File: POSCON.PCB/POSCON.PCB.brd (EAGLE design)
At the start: 55.8 x 40.9 mm, 21 parts, among them J1-PROG RJ45-8, J2 RJ45-8, U1 MC9S08QG-DT, U3 RS485SOIC, U4 PCA9552

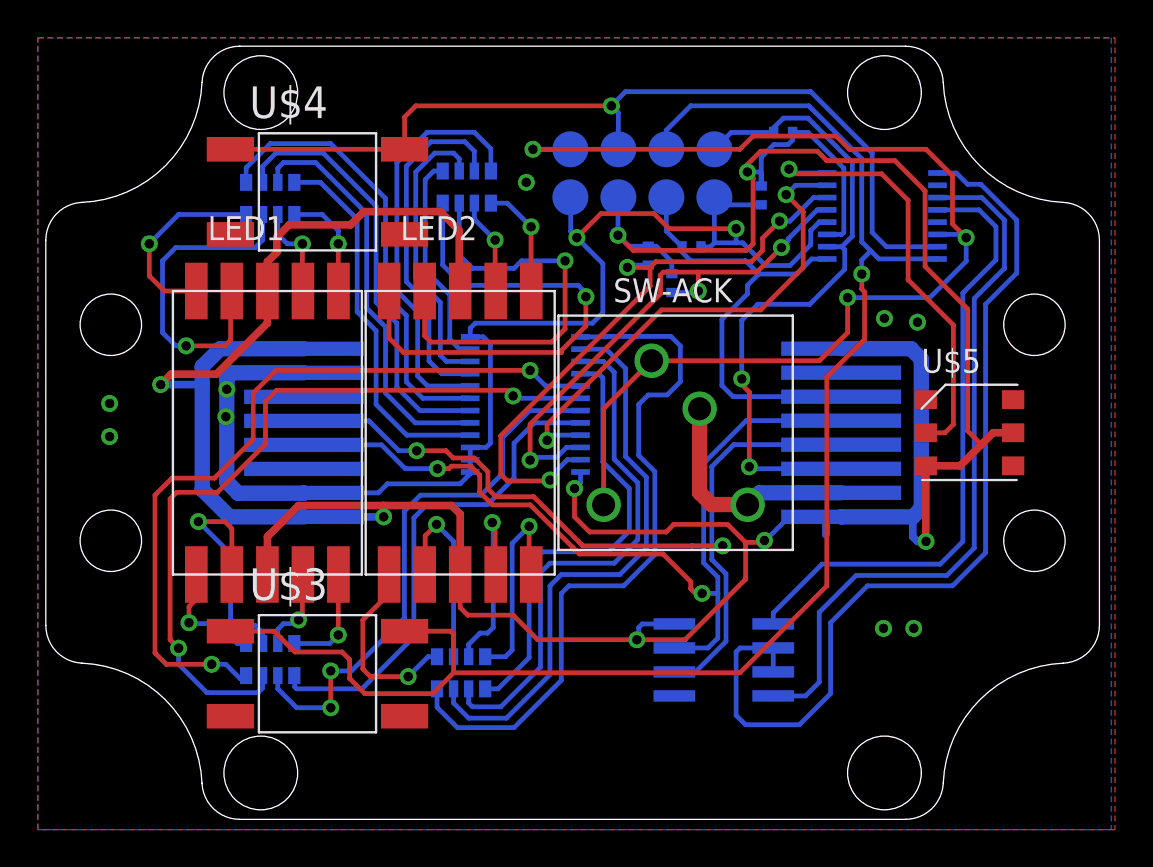
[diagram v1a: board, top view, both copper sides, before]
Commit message: KW2 antenna, LasCon panel, PosCon fiducials
Added vertical MMCX connector to KW2 design & library; added panelized
version of LasCon (old and new design); added Adafruit library and
fiducials to new PosCon
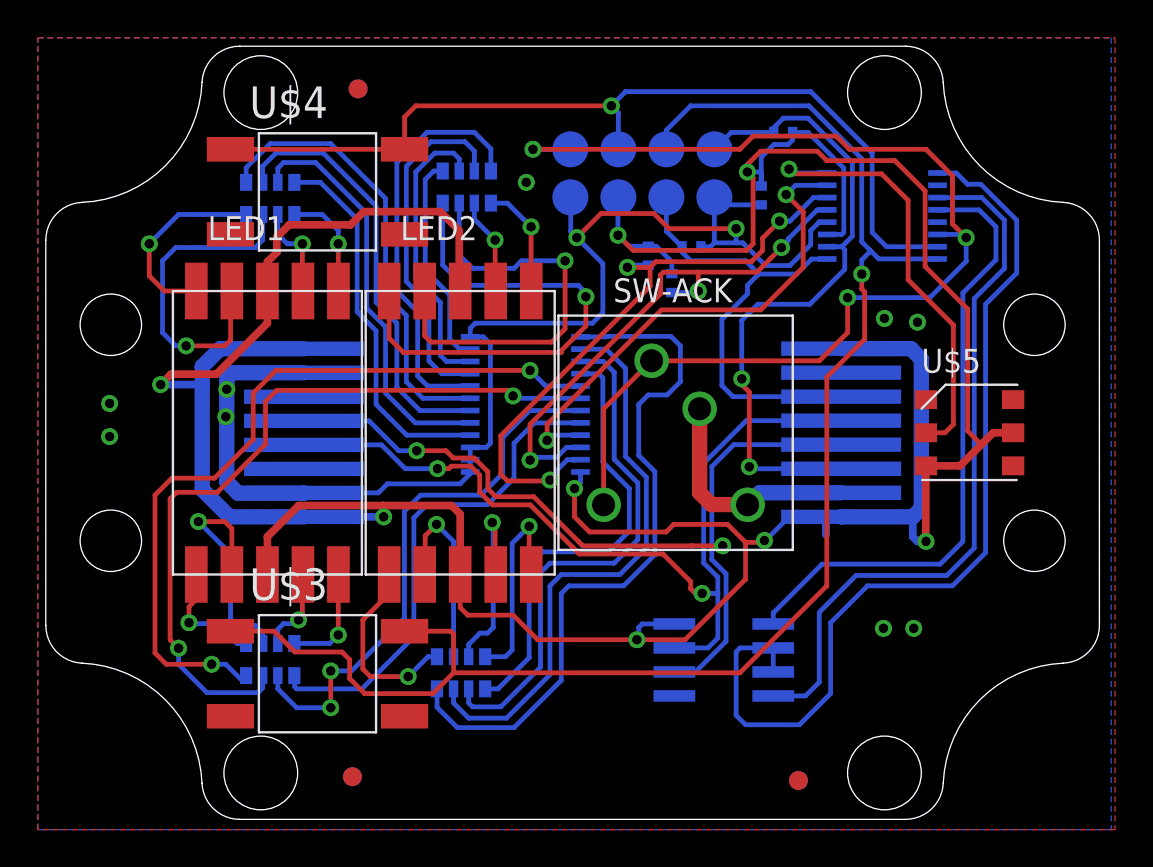
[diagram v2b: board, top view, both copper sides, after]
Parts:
- added U$1, U$2, U$6, U$7, U$8, U$9: FIDUCIAL, adafruit:FIDUCIAL_1MM
